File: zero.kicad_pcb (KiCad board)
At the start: 2 copper layers, 266 x 76 mm, 71 parts, among them SW101 SW_Push, SW102 SW_Push, SW103 SW_Push, SW104 SW_Push, SW105 SW_Push, SW106 SW_Push, SW107 SW_Push, SW108 SW_Push, SW109 SW_Push, SW110 SW_Push, SW111 SW_Push, SW112 SW_Push, SW201 SW_Push, SW202 SW_Push, SW203 SW_Push, SW204 SW_Push, SW205 SW_Push, SW206 SW_Push, SW207 SW_Push, SW208 SW_Push, SW209 SW_Push, SW210 SW_Push, SW211 SW_Push, SW212 SW_Push, SW404 SW_Push, SW405 SW_Push, SW406 SW_Push, SW407 SW_Push, SW408 SW_Push, SW409 SW_Push, U1 Pico

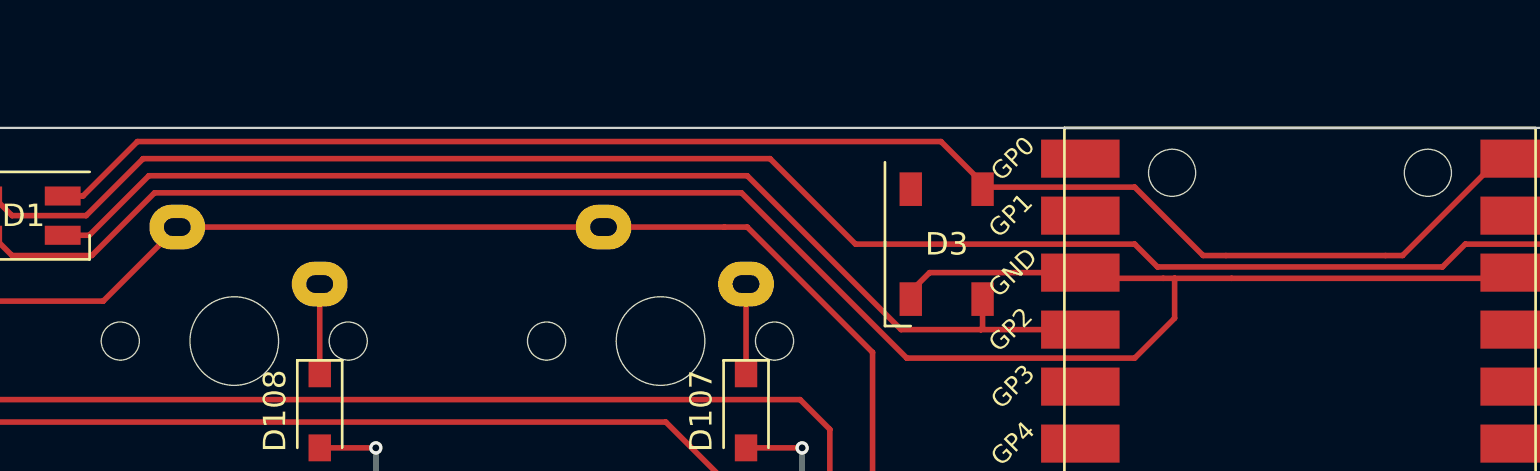
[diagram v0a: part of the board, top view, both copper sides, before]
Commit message: Remove WS2812B
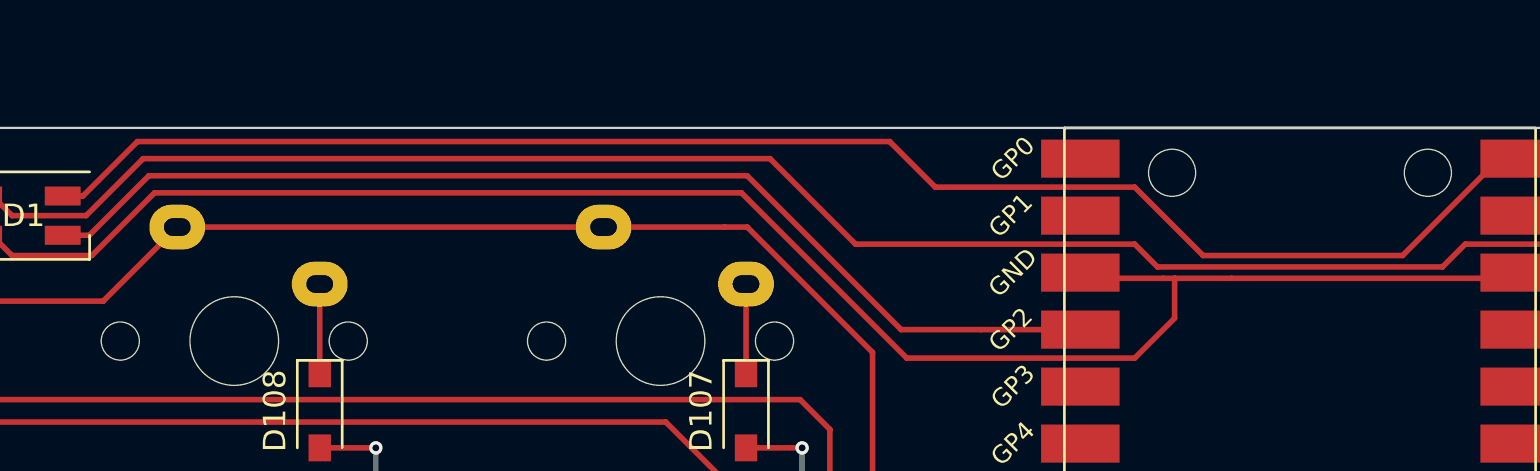
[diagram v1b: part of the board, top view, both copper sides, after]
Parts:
- removed D3: WS2812B, LED_SMD:LED_WS2812B_PLCC4_5.0x5.0mm_P3.2mm
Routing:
- net GND: track 138.2 -> 129.0 mm
- net /RGB: track 51.6 -> 50.2 mm

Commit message: Extend ground pour to both sides
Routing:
- added copper zone on F.Cu, net GND
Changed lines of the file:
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@@
   (segment (start 23.42 69.04) (end 42.42 69.04) (width 0.25) (layer "F.Cu") (net 64))
   (segment (start 8.89 47.09) (end 10.795 47.09) (width 0.25) (layer "F.Cu") (net 64))
-  (zone (net 61) (net_name "GND") (layer "B.Cu") (hatch edge 0.508)
+  (zone (net 61) (net_name "GND") (layers F&B.Cu) (hatch edge 0.508)
     (connect_pads yes (clearance 0.2))
     (min_thickness 0.5) (filled_areas_thickness no)

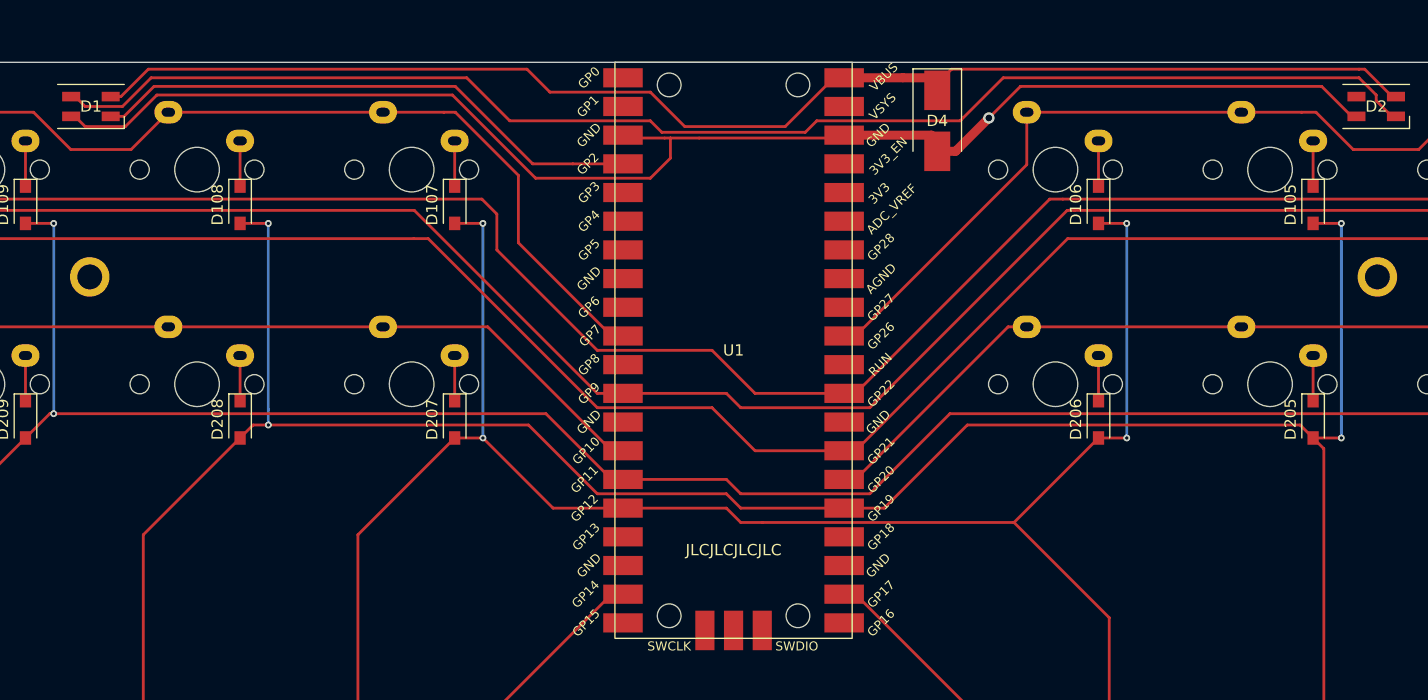
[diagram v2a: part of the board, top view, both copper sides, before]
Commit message: Add edge clearance for ground pours
- Change mounting holes for pico to PTHs
- Connect RGB power to VSYS instead of VBUS (this gives us more
  clearance around the mounting holes and should work equally well)
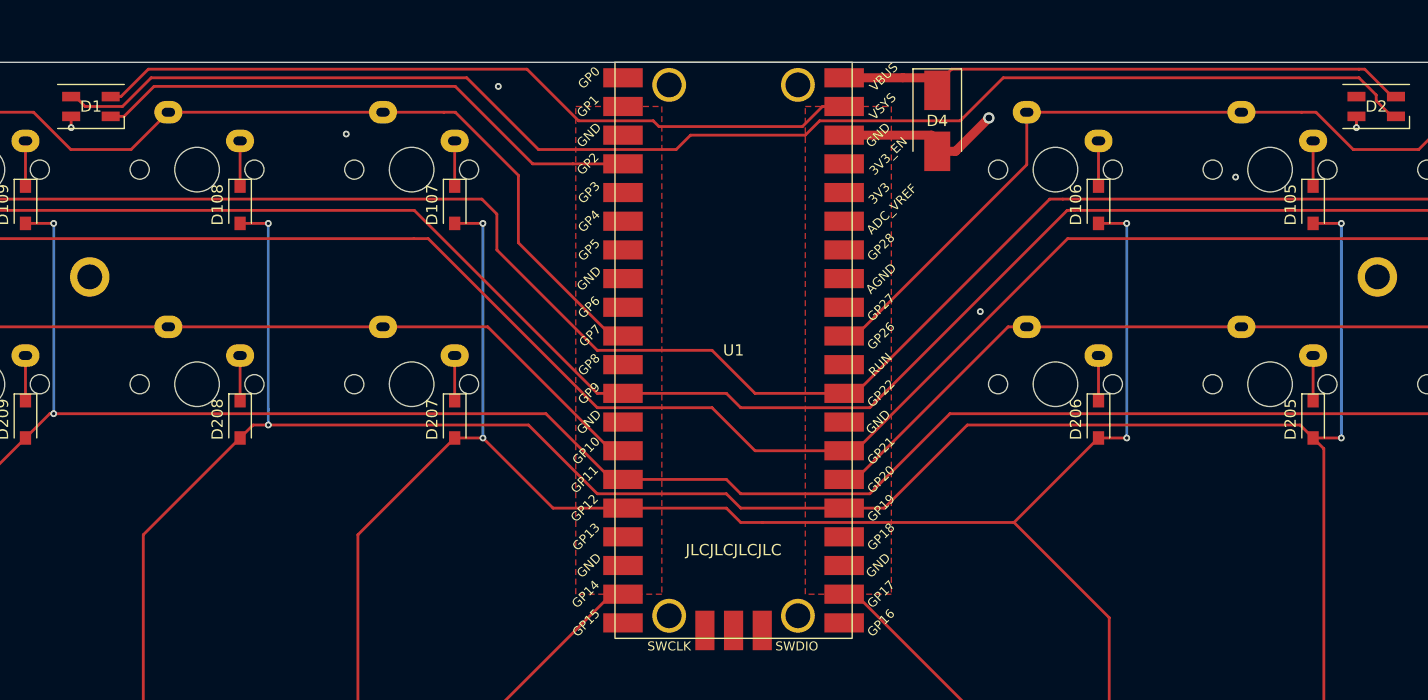
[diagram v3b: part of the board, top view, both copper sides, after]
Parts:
- added H10: MountingHole Pico, footprints:M2 Hole Pico, F.Cu at (5.70, 2.00)
- added H7: MountingHole Pico, footprints:M2 Hole Pico, F.Cu at (-5.70, 49.0)
- added H8: MountingHole Pico, footprints:M2 Hole Pico, F.Cu at (5.70, 49.0)
- added H9: MountingHole Pico, footprints:M2 Hole Pico, F.Cu at (-5.70, 2.00)
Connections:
- D1 pad 4: VBUS -> +5V
- U1 pad 13: unconnected-(U1-Pad13) -> GND
- U1 pad 18: unconnected-(U1-Pad18) -> GND
- U1 pad 23: unconnected-(U1-Pad23) -> GND
- U1 pad 28: unconnected-(U1-Pad28) -> GND
- U1 pad 33: unconnected-(U1-Pad33) -> GND
- U1 pad 39: unconnected-(U1-Pad39) -> +5V
- U1 pad 8: unconnected-(U1-Pad8) -> GND
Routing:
- net GND: track 129.0 -> 18.1 mm, vias 1 -> 7
- net VBUS: track 121.0 -> 52.1 mm
- net +5V: track 0.00 -> 67.9 mm
- net /DIN_DOUT: track 124.4 -> 125.7 mm
